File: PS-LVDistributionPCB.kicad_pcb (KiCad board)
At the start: 2 copper layers, 161 x 63 mm, 80 parts, among them J1 NON CRIT OUT, J10 CRIT OUT, J12 NON CRIT OUT, J13 NON CRIT OUT, J14 NON CRIT OUT, J15 NON CRIT OUT, J16 NON CRIT OUT, J17 NON CRIT OUT, J18 NON CRIT OUT, J19 NON CRIT OUT, J2 NON CRIT OUT, J20 NON CRIT OUT, J21 CRIT, J22 CRIT OUT, J3 CRIT OUT, J4 NON CRIT OUT, J5 NON CRIT, J6 CRIT OUT, J7 CRIT OUT, J8 CRIT OUT, J9 CRIT OUT

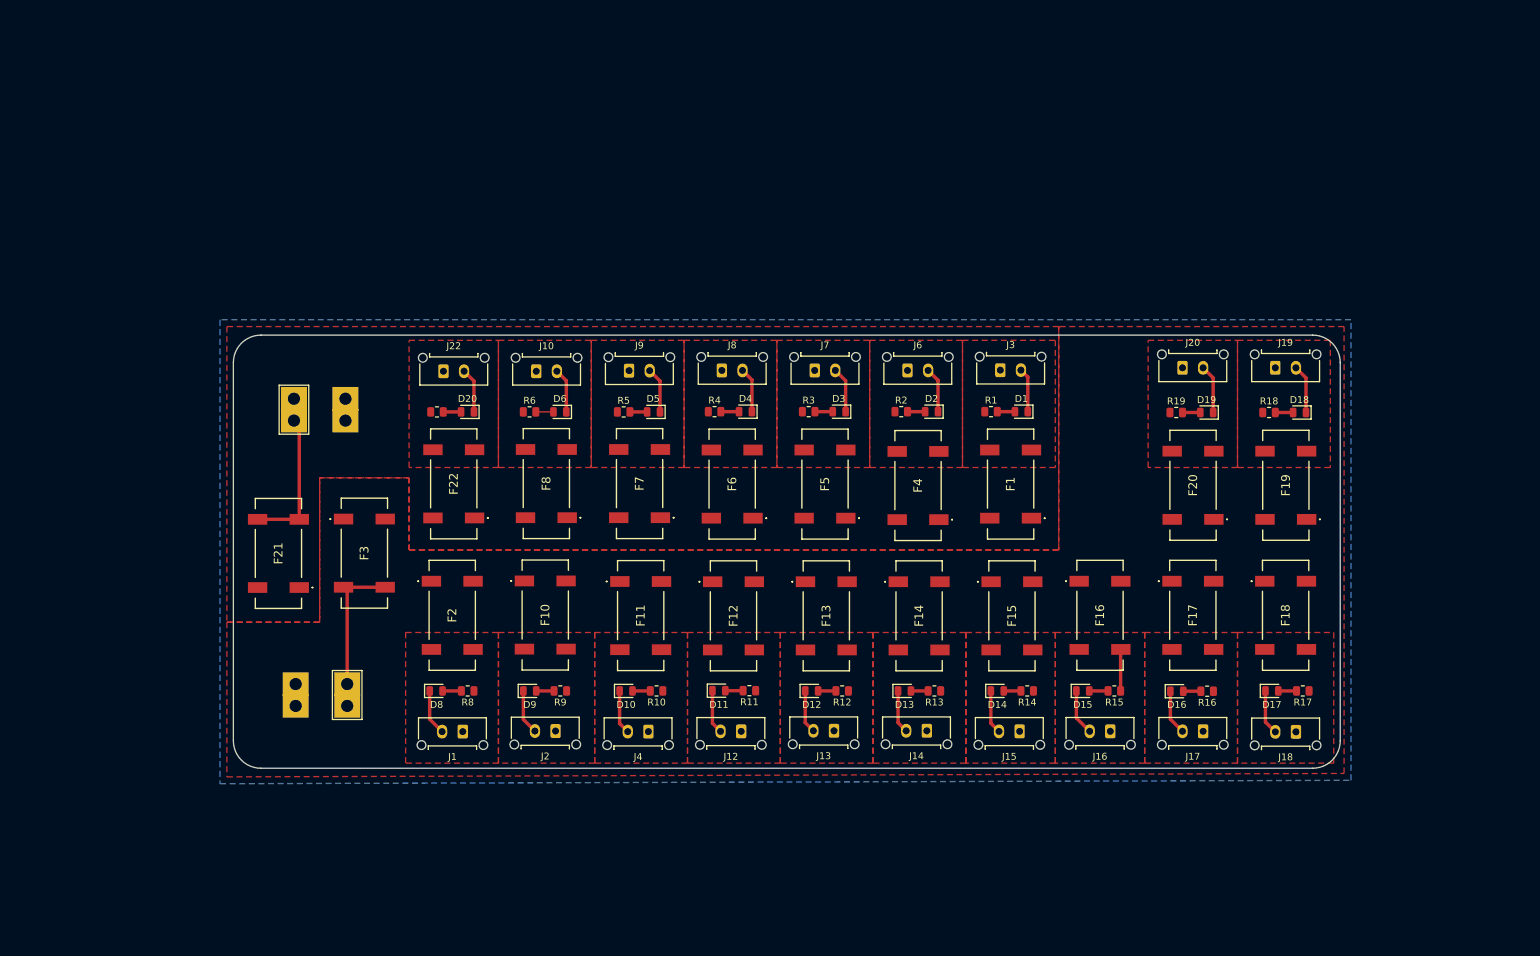
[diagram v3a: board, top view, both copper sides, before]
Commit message: rearranged fuses on the back and and connectors on the front for improved waterproofing
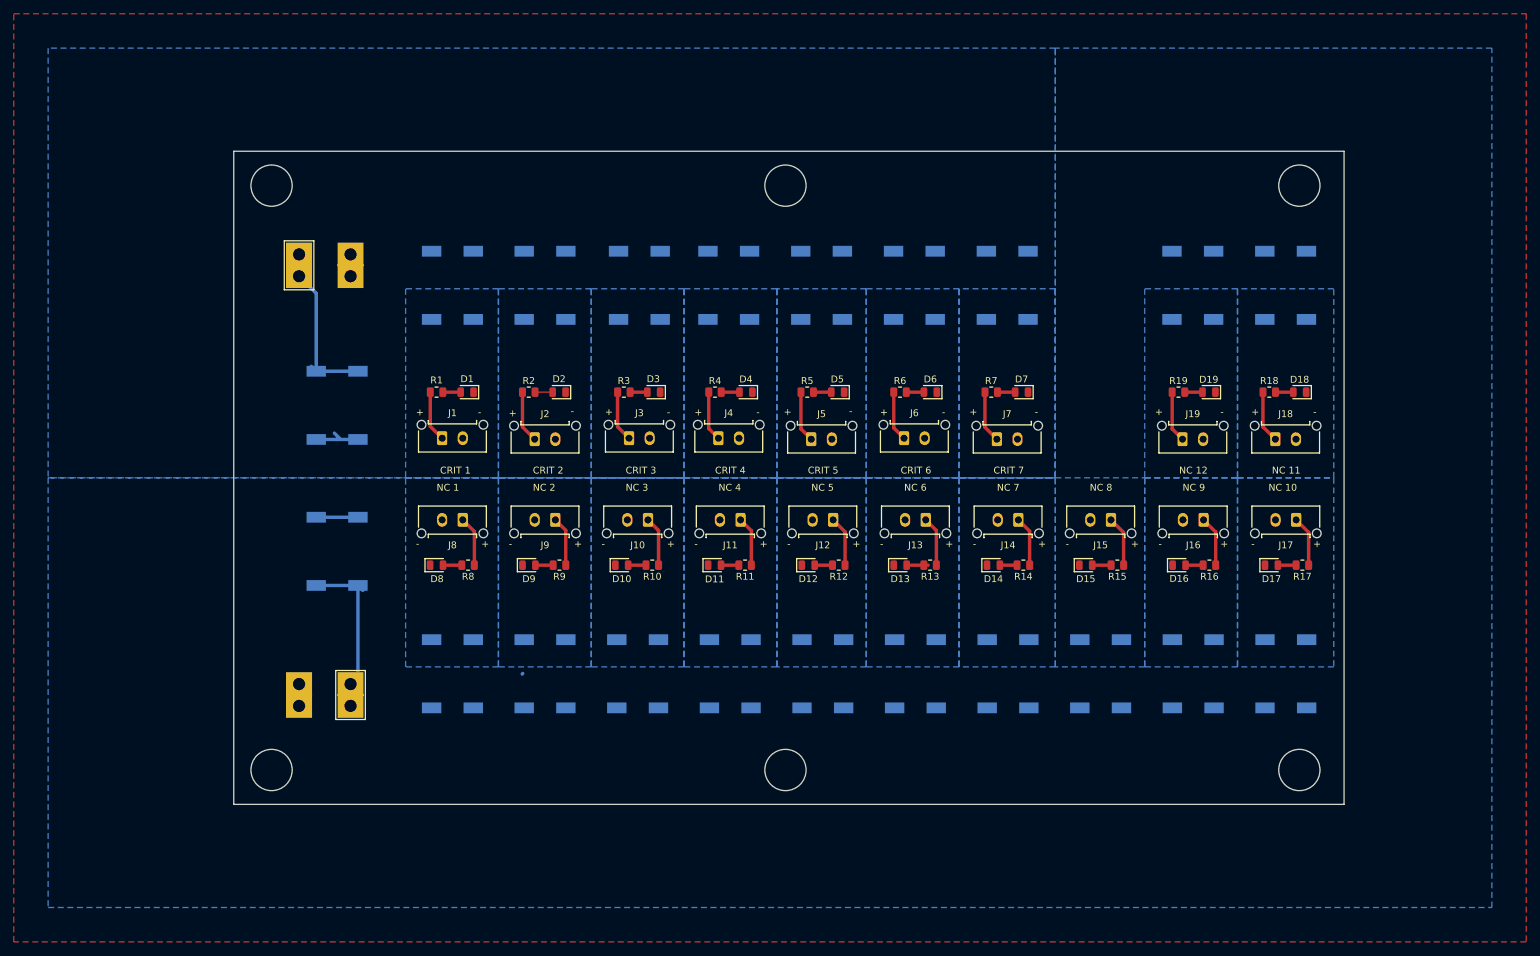
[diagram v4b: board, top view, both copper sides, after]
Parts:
- added G***: LOGO, logos:UTSVT logo small, B.Cu at (77.0, 103.0)
- F1: renamed from F22; moved to B.Cu
- F10: renamed from F11; moved to B.Cu
- F11: renamed from F12; moved to B.Cu
- F12: renamed from F13; moved to B.Cu
- F13: renamed from F14; moved to B.Cu
- F14: renamed from F15; moved to B.Cu
- F15: renamed from F16; moved to B.Cu
- F16: renamed from F17; moved to B.Cu
- F17: renamed from F18; moved to B.Cu
- F18: renamed from F19; moved to B.Cu
- F19: renamed from F20; moved to B.Cu
- F2: renamed from F8; moved to B.Cu
- F20: renamed from F21; moved to B.Cu
- F21: renamed from F3; moved to B.Cu
- F3: renamed from F7; moved to B.Cu
- F4: renamed from F6; moved to B.Cu
- F5: moved to B.Cu
- F6: renamed from F4; moved to B.Cu
- F7: renamed from F1; moved to B.Cu
- F8: renamed from F2; moved to B.Cu
- F9: renamed from F10; moved to B.Cu
- R1: renamed from R20; value 505 -> 1k
- R10, R11, R12, R13, R14, R15, R16, R17, R18, R19, R4, R8, R9: value 505 -> 1k
- R2: renamed from R6; value 505 -> 1k
- R3: renamed from R5; value 505 -> 1k
- R5: renamed from R3; value 505 -> 1k
- R6: renamed from R2; value 505 -> 1k
- R7: renamed from R1; value 505 -> 1k
- moved J17 30.8 mm to (226.5, 98.6)
- moved J10 30.8 mm to (132.2, 98.6)
- moved J8 30.8 mm to (105.3, 98.6)
- moved J14 30.8 mm to (186.1, 98.6)
- moved J11 30.8 mm to (145.7, 98.6)
- moved J15 30.8 mm to (199.6, 98.6)
- moved J16 30.8 mm to (213.1, 98.6)
- moved J9 30.7 mm to (118.8, 98.6)
- moved J13 30.7 mm to (172.7, 98.6)
- moved J12 30.7 mm to (159.2, 98.6)
- moved F6 29.1 mm to (171.0, 64.5), turned to -90 degrees
- moved F18 29.1 mm to (225.0, 64.5), turned to -90 degrees
- moved F19 29.1 mm to (211.5, 64.5), turned to -90 degrees
- moved F4 28.9 mm to (144.0, 64.5), turned to -90 degrees
- moved F5 28.9 mm to (157.5, 64.5), turned to -90 degrees
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- renumbered D20 to D1, D6 to D2, D5 to D3, D3 to D5, D2 to D6, D1 to D7, J22 to J1, J4 to J10, J12 to J11, J13 to J12, J14 to J13, J15 to J14, J16 to J15, J17 to J16, J18 to J17, J19 to J18, J20 to J19, J10 to J2, J21 to J20, J5 to J21, J9 to J3, J8 to J4, J7 to J5, J3 to J7, J1 to J8, J2 to J9
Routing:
- net GND: track 124.8 -> 0.50 mm
- net Net-(J2-Pin_1): track 0.00 -> 7.58 mm
- net Net-(J7-Pin_1): track 0.00 -> 7.56 mm
- net Net-(J5-Pin_1): track 0.41 -> 7.87 mm
- net Net-(J1-Pin_1): track 0.00 -> 7.41 mm
- net Net-(J6-Pin_1): track 0.00 -> 7.32 mm
- net Net-(J12-Pin_1): track 0.00 -> 7.30 mm
- net Net-(J4-Pin_1): track 0.00 -> 7.29 mm
- net Net-(J16-Pin_1): track 0.04 -> 7.32 mm
- net Net-(J11-Pin_1): track 0.00 -> 7.24 mm
- net Net-(J10-Pin_1): track 0.00 -> 7.22 mm
- net +12V_CRIT: track 0.00 -> 7.16 mm
- net Net-(J18-Pin_1): track 0.46 -> 7.58 mm
- net Net-(J14-Pin_1): track 0.15 -> 7.26 mm
- net Net-(J3-Pin_1): track 0.28 -> 7.39 mm
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- added copper zone on B.Cu, net +12V_CRIT
- added copper zone on B.Cu, net +12V_NON
- added copper zone on F.Cu, net GND
- added copper zone on B.Cu, net Net-(J1-Pin_1)
- added copper zone on B.Cu, net Net-(J10-Pin_1)
- added copper zone on B.Cu, net Net-(J11-Pin_1)
- added copper zone on B.Cu, net Net-(J12-Pin_1)
- added copper zone on B.Cu, net Net-(J13-Pin_1)
- added copper zone on B.Cu, net Net-(J14-Pin_1)
- added copper zone on B.Cu, net Net-(J15-Pin_1)
- added copper zone on B.Cu, net Net-(J16-Pin_1)
- added copper zone on B.Cu, net Net-(J17-Pin_1)
- added copper zone on B.Cu, net Net-(J18-Pin_1)
- added copper zone on B.Cu, net Net-(J19-Pin_1)
- added copper zone on B.Cu, net Net-(J2-Pin_1)
- added copper zone on B.Cu, net Net-(J3-Pin_1)
- added copper zone on B.Cu, net Net-(J4-Pin_1)
- added copper zone on B.Cu, net Net-(J5-Pin_1)
- added copper zone on B.Cu, net Net-(J6-Pin_1)
- added copper zone on B.Cu, net Net-(J7-Pin_1)
- added copper zone on B.Cu, net Net-(J8-Pin_1)
- added copper zone on B.Cu, net Net-(J9-Pin_1)
- removed copper zone on F.Cu, net +12V_CRIT
- removed copper zone on F.Cu, net +12V_NON
- removed copper zone on B.Cu, net GND
- removed copper zone on F.Cu, net Net-(J1-Pin_1)
- removed copper zone on F.Cu, net Net-(J10-Pin_1)
- removed copper zone on F.Cu, net Net-(J11-Pin_1)
- removed copper zone on F.Cu, net Net-(J12-Pin_1)
- removed copper zone on F.Cu, net Net-(J13-Pin_1)
- removed copper zone on F.Cu, net Net-(J14-Pin_1)
- removed copper zone on F.Cu, net Net-(J15-Pin_1)
- removed copper zone on F.Cu, net Net-(J16-Pin_1)
- removed copper zone on F.Cu, net Net-(J17-Pin_1)
- removed copper zone on F.Cu, net Net-(J18-Pin_1)
- removed copper zone on F.Cu, net Net-(J19-Pin_1)
- removed copper zone on F.Cu, net Net-(J2-Pin_1)
- removed copper zone on F.Cu, net Net-(J3-Pin_1)
- removed copper zone on F.Cu, net Net-(J4-Pin_1)
- removed copper zone on F.Cu, net Net-(J5-Pin_1)
- removed copper zone on F.Cu, net Net-(J6-Pin_1)
- removed copper zone on F.Cu, net Net-(J7-Pin_1)
- removed copper zone on F.Cu, net Net-(J8-Pin_1)
- removed copper zone on F.Cu, net Net-(J9-Pin_1)
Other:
- board size 161 x 63 mm -> 161.5 x 95 mm
- board text added: "+"
- board text added: "-"
- board text added: "CRIT 1"
- board text added: "CRIT 2"
- board text added: "CRIT 3"
- board text added: "CRIT 4"
- board text added: "CRIT 5"
- board text added: "CRIT 6"
- board text added: "CRIT 7"
- board text added: "CRIT IN"
- board text added: "LV Distribution PCB Surabhi Karighattam 2025"
- board text added: "NC 1"
- board text added: "NC 10"
- board text added: "NC 11"
- board text added: "NC 12"
- board text added: "NC 2"
- board text added: "NC 3"
- board text added: "NC 4"
- board text added: "NC 5"
- board text added: "NC 6"
- board text added: "NC 7"
- board text added: "NC 8"
- board text added: "NC 9"
- board text added: "NC IN"
- board text added: "R1"

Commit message: reoriented fuses horizontally to fit enclosure dimensions
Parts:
- moved G*** 140.7 mm to (216.6, 85.2), turned to 180 degrees
- moved J20 40.2 mm to (58.5, 93.0)
- moved F21 34.9 mm to (62.0, 127.5), turned to 0 degrees
- moved F18 34.6 mm to (254.6, 82.5), turned to 180 degrees
- moved R18 32.9 mm to (252.7, 93.5)
- moved D18 32.6 mm to (256.8, 93.5)
- moved J18 32.2 mm to (253.1, 99.6)
- moved J17 31.9 mm to (256.1, 110.5)
- moved D17 31.7 mm to (252.6, 116.5)
- moved R17 31.0 mm to (256.3, 116.5)
- moved F17 30.3 mm to (254.6, 127.5), turned to 0 degrees
- moved F19 30.0 mm to (235.6, 82.4), turned to 180 degrees
- moved R19 27.7 mm to (233.6, 93.5)
- moved D19 27.4 mm to (237.7, 93.5)
- moved J19 27.2 mm to (234.1, 99.6)
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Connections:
- net +12V_CRIT renamed +12V CRIT
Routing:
- net +12V_NON: track 6.13 -> 72.7 mm
- net +12V CRIT: track 7.16 -> 42.4 mm
- net Net-(J20-Pin_1): track 21.9 -> 0.00 mm
- net Net-(J21-Pin_1): track 21.9 -> 0.00 mm
- net Net-(J5-Pin_1): track 7.87 -> 6.55 mm
- net Net-(J2-Pin_1): track 7.58 -> 6.55 mm
- net Net-(J7-Pin_1): track 7.56 -> 6.55 mm
- net Net-(J18-Pin_1): track 7.58 -> 6.63 mm
- net Net-(J15-Pin_1): track 7.35 -> 6.43 mm
- net Net-(J17-Pin_1): track 7.34 -> 6.43 mm
- net Net-(J16-Pin_1): track 7.32 -> 6.43 mm
- net Net-(D8-A): track 2.74 -> 1.86 mm
- net Net-(D15-A): track 2.74 -> 1.86 mm
- net Net-(J12-Pin_1): track 7.30 -> 6.43 mm
- net Net-(J1-Pin_1): track 7.41 -> 6.55 mm
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- added copper zone on B.Cu, net Net-(J20-Pin_1)
- added copper zone on B.Cu, net Net-(J21-Pin_1)
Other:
- board size 161.5 x 95 mm -> 226 x 70 mm
- board text added: "LV Distribution Surabhi Karighattam 2025"
- board text removed: "LV Distribution PCB Surabhi Karighattam 2025"
- board text removed: "R1"
